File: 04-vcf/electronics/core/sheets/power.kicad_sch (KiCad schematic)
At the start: 9 parts, among them J3 Conn_02x05_Odd_Even, J4 Conn_01x02, J5 Conn_02x03_Odd_Even

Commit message: Started VCF
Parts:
- renumbered C23 to C21, C24 to C22, D6 to D11, D7 to D12, J5 to J6, J4 to J7, J3 to J8, TP12 to TP1, TP13 to TP2
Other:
- moved on the sheet: C21, C22, D11, D12, J6, J7, J8, TP1, TP2

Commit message: Added production files to VCF core
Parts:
- J6: Mouser Part no. 200-TSW10307TD -> (none); Part no. (none) -> 200-TSW10307TD
- J7: Mouser Part no. 200-HTSW10207TS -> (none); Part no. (none) -> 200-HTSW10207TS
- J8: Mouser Part no. 571-5103310-1 -> (none); Part no. (none) -> 571-5103310-1
- TP1, TP2: Vendor (none) -> X
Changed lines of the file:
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@@
+			)
+		)
+		(property "Arwill" ""
+			(at 219.71 86.36 0)
+			(effects
+				(font
+					(size 1.27 1.27)
+				)
+				(hide yes)
+			)
+		)
+		(property "Hestore" ""
+			(at 219.71 86.36 0)
+			(effects
+				(font
+					(size 1.27 1.27)
+				)
+				(hide yes)
 			)
 		)
@@
 		)
 		(property "CHECKED" "YES"
+			(at 163.83 101.6 0)
+			(effects
+				(font
+					(size 1.27 1.27)
+				)
+				(hide yes)
+			)
+		)
+		(property "Arwill" ""
+			(at 163.83 101.6 0)
+			(effects
+				(font
+					(size 1.27 1.27)
+				)
+				(hide yes)
+			)
+		)
+		(property "Hestore" ""
 			(at 163.83 101.6 0)
 			(effects
@@
 			)
 		)
-		(property "Mouser Part no." "200-TSW10307TD"
+		(property "Arwill" ""
+			(at 77.47 87.63 0)
+			(effects
+				(font
+					(size 1.27 1.27)
+				)
+				(hide yes)
+			)
+		)
+		(property "Hestore" ""
+			(at 77.47 87.63 0)
+			(effects
+				(font
+					(size 1.27 1.27)
+				)
+				(hide yes)
+			)
+		)
+		(property "Part no." "200-TSW10307TD"
 			(at 77.47 87.63 0)
 			(effects
@@
 		)
 		(property "CHECKED" "YES"
+			(at 219.71 93.98 0)
+			(effects
+				(font
+					(size 1.27 1.27)
+				)
+				(hide yes)
+			)
+		)
+		(property "Arwill" ""
+			(at 219.71 93.98 0)
+			(effects
+				(font
+					(size 1.27 1.27)
+				)
+				(hide yes)
+			)
+		)
+		(property "Hestore" ""
 			(at 219.71 93.98 0)
 			(effects
@@
 			)
 		)
-		(property "Mouser Part no." "571-5103310-1"
+		(property "Arwill" ""
+			(at 144.78 92.71 0)
+			(effects
+				(font
+					(size 1.27 1.27)
+				)
+				(hide yes)
+			)
+		)
+		(property "Hestore" ""
+			(at 144.78 92.71 0)
+			(effects
+				(font
+					(size 1.27 1.27)
+				)
+				(hide yes)
+			)
+		)
+		(property "Part no." "571-5103310-1"
 			(at 144.78 92.71 0)
 			(effects
@@
 			)
 		)
+		(property "Arwill" ""
+			(at 162.56 80.01 0)
+			(effects
+				(font
+					(size 1.27 1.27)
+				)
+				(hide yes)
+			)
+		)
+		(property "Hestore" ""
+			(at 162.56 80.01 0)
+			(effects
+				(font
+					(size 1.27 1.27)
+				)
+				(hide yes)
+			)
+		)
 		(pin "2"
 		)
@@
 			)
 		)
+		(property "Arwill" ""
+			(at 176.53 102.87 0)
+			(effects
+				(font
+					(size 1.27 1.27)
+				)
+				(hide yes)
+			)
+		)
+		(property "Hestore" ""
+			(at 176.53 102.87 0)
+			(effects
+				(font
+					(size 1.27 1.27)
+				)
+				(hide yes)
+			)
+		)
+		(property "Vendor" "X"
+			(at 176.53 102.87 0)
+			(effects
+				(font
+					(size 1.27 1.27)
+				)
+				(hide yes)
+			)
+		)
 		(pin "1"
 		)
@@
 			)
 		)
-		(property "Mouser Part no." "200-HTSW10207TS"
+		(property "Arwill" ""
+			(at 81.28 104.14 0)
+			(effects
+				(font
+					(size 1.27 1.27)
+				)
+				(hide yes)
+			)
+		)
+		(property "Hestore" ""
+			(at 81.28 104.14 0)
+			(effects
+				(font
+					(size 1.27 1.27)
+				)
+				(hide yes)
+			)
+		)
+		(property "Part no." "200-HTSW10207TS"
 			(at 81.28 104.14 0)
 			(effects
@@
 			(at 176.53 78.74 0)
 			(effects
+				(font
+					(size 1.27 1.27)
+				)
+				(hide yes)
+			)
+		)
+		(property "Arwill" ""
+			(at 176.53 78.74 0)
+			(effects
+				(font
+					(size 1.27 1.27)
+				)
+				(hide yes)
+			)
+		)
+		(property "Hestore" ""
+			(at 176.53 78.74 0)
+			(effects
+				(font
+					(size 1.27 1.27)
+				)
+				(hide yes)
+			)
+		)
+		(property "Vendor" "X"
+			(at 176.53 78.74 0)
+			(effects

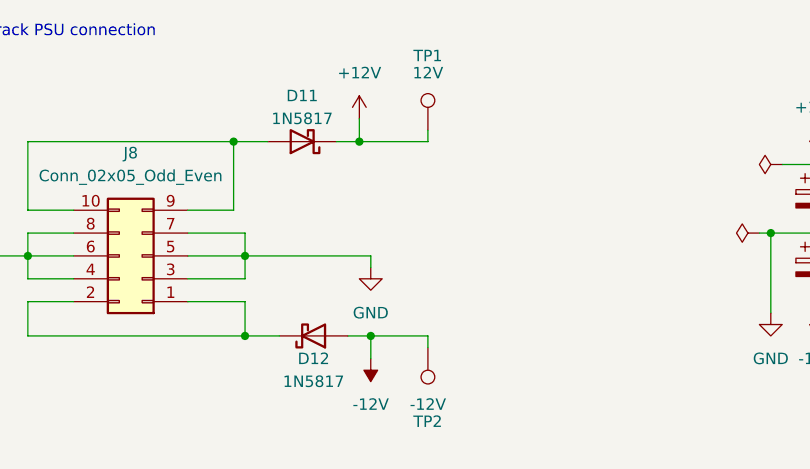
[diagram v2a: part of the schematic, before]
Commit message: Redesigned VCF PCB to avoid crosstalk
- There's been quite a bit of crosstalk between the input and output of the VCF module. This PCB design attemtps to separate the input and output so that the crosstalk is minimized.
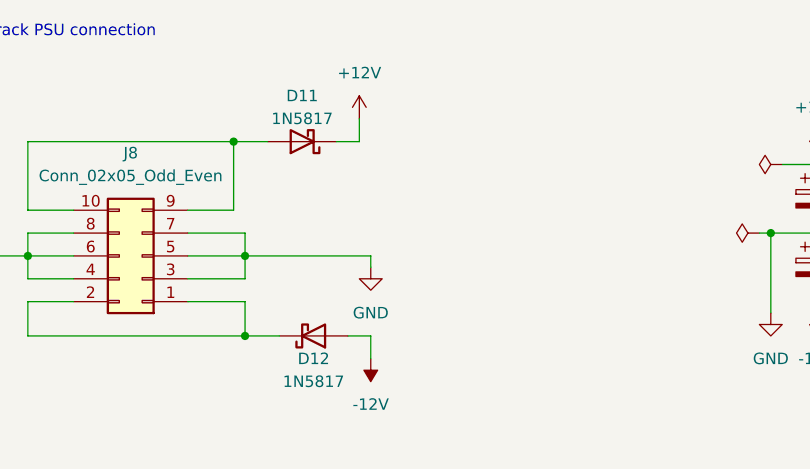
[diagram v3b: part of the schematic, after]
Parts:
- removed TP1: 12V, TestPoint:TestPoint_THTPad_2.0x2.0mm_Drill1.0mm, symbol Connector:TestPoint
- removed TP2: -12V, TestPoint:TestPoint_THTPad_2.0x2.0mm_Drill1.0mm, symbol Connector:TestPoint
